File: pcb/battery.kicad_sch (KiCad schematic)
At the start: 16 parts, among them J1 Battery_JST, J2 Battery_JST, Q1 FS8205A, U1 IP2326, U2 HY2120CB, U5 TPS54308

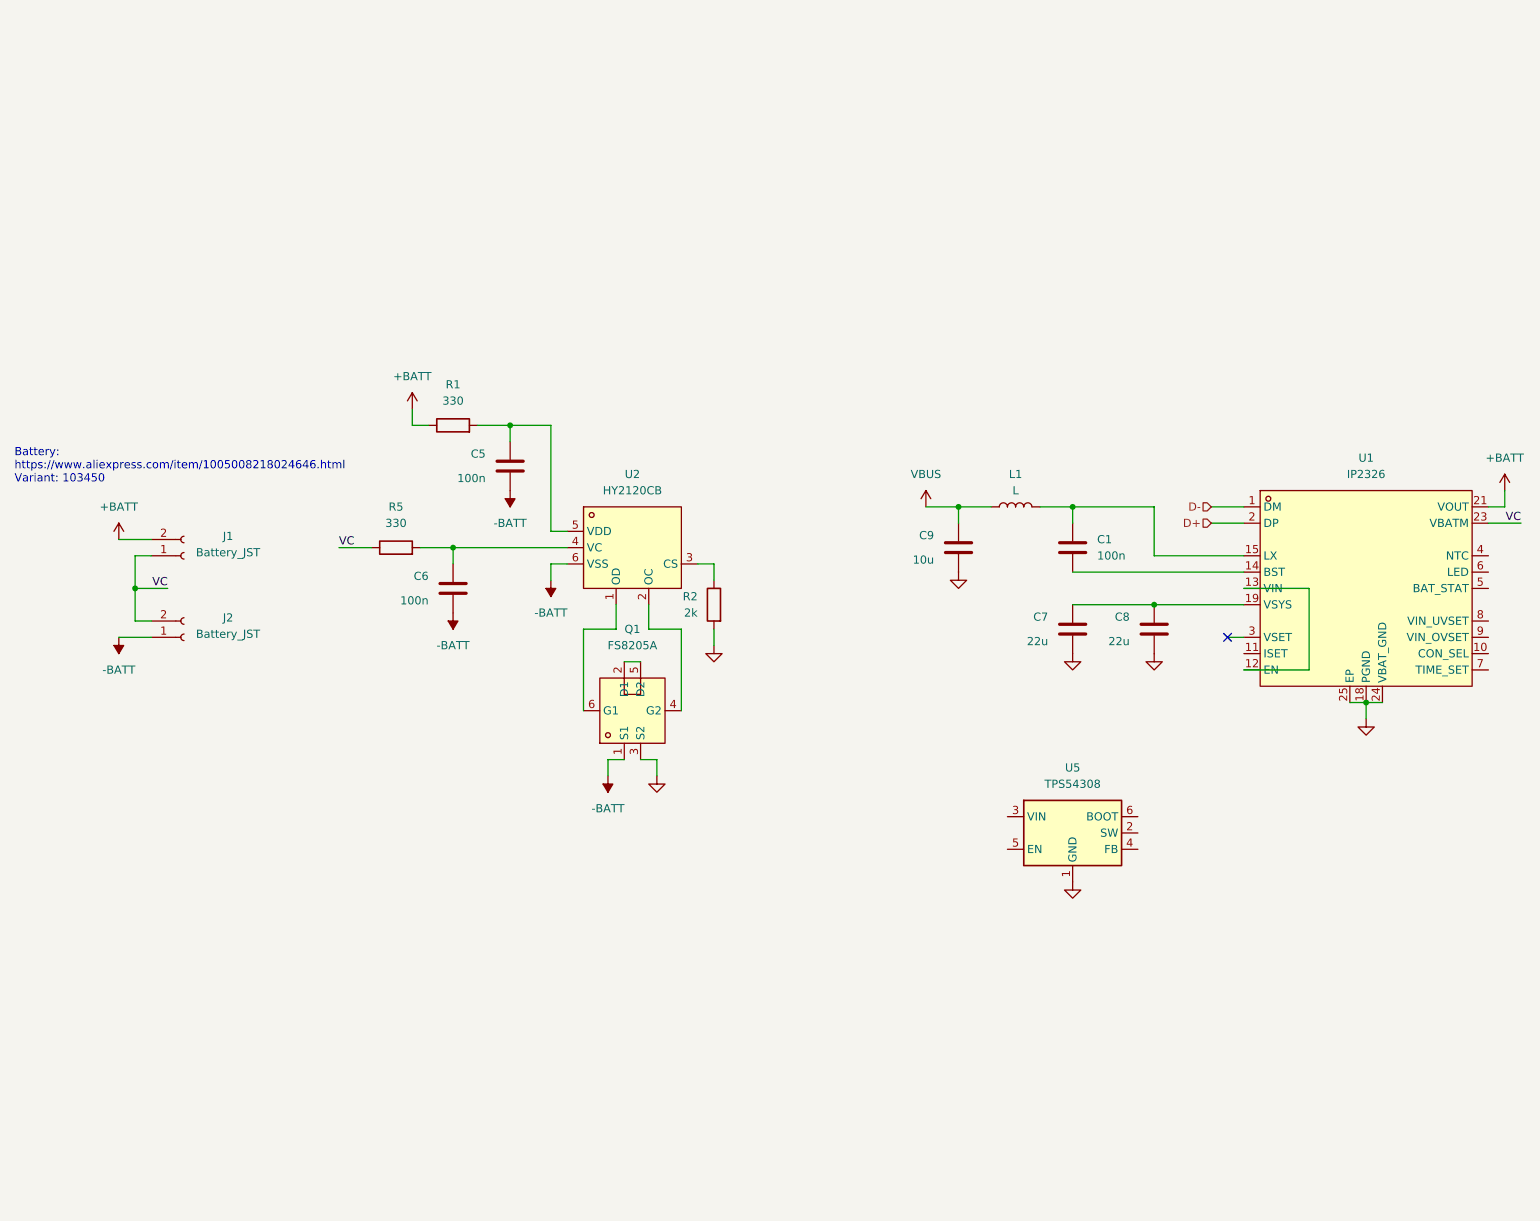
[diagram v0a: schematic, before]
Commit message: add neopixel sheet, finished battery and main circuitry
Signed-off-by: Toby Cm <toby@vsus.app>
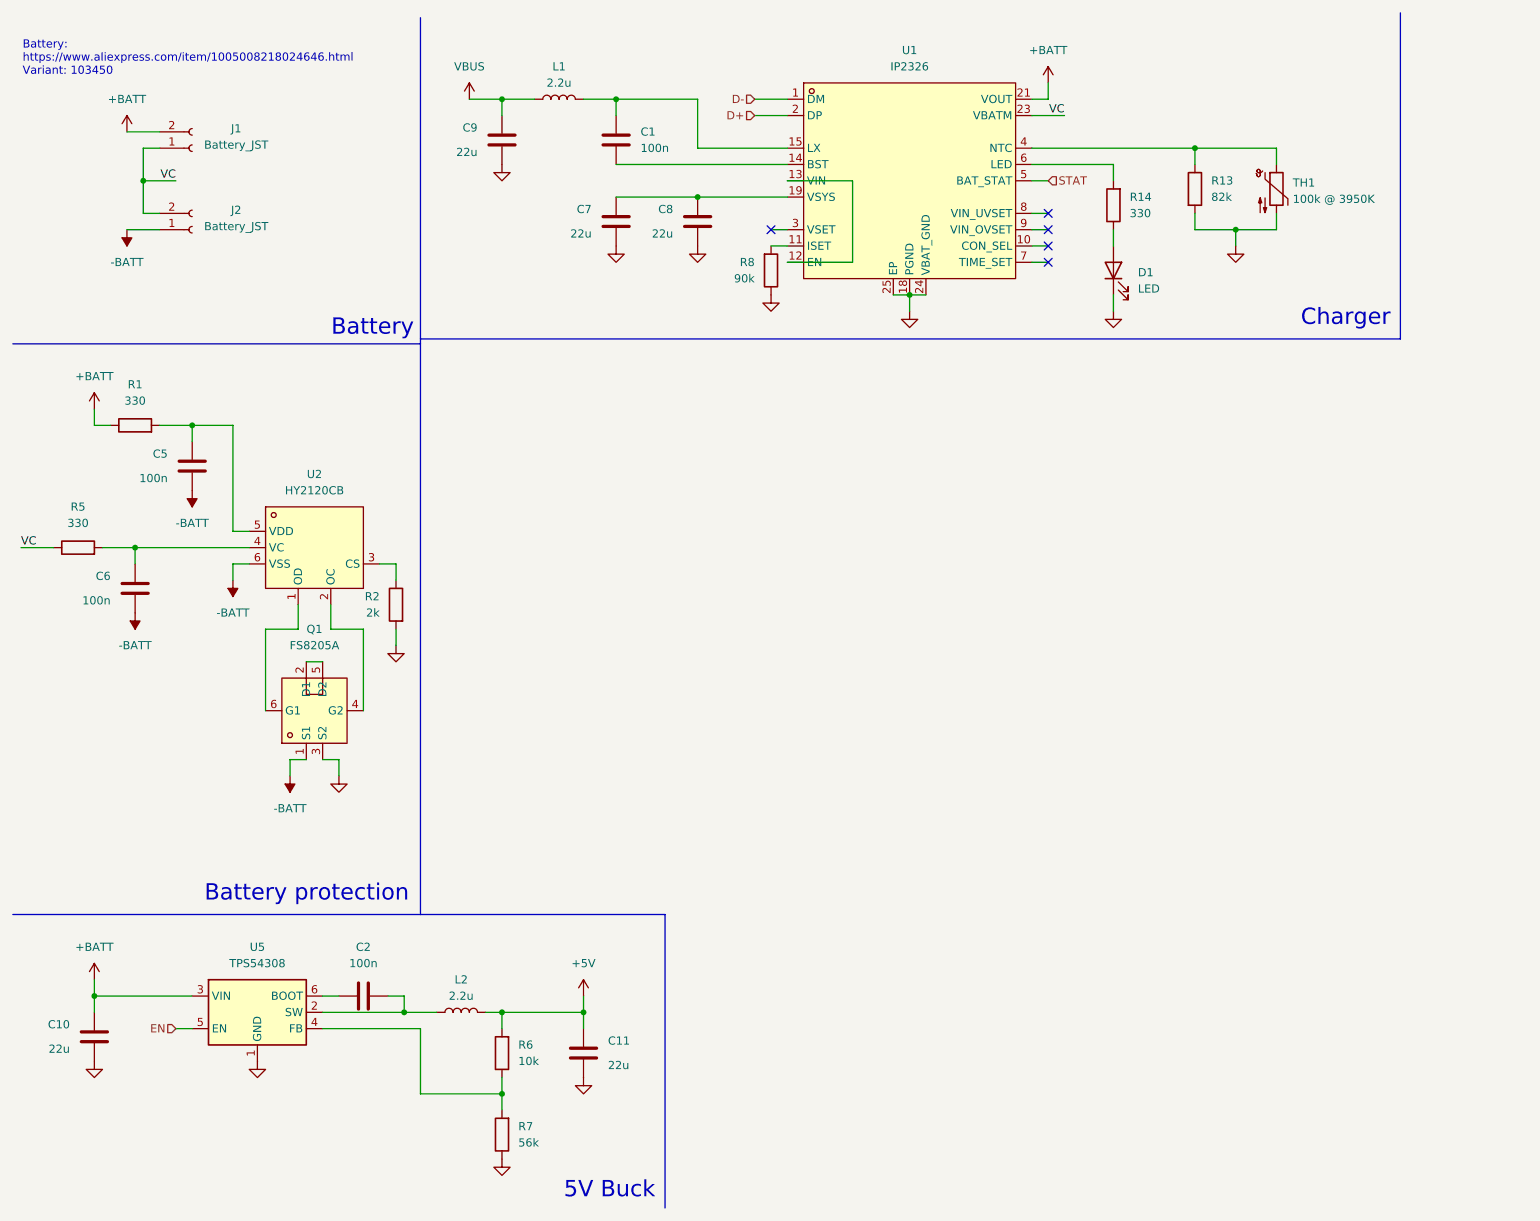
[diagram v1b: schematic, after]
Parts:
- added C10, C11: 22u, Capacitor_SMD:C_0805_2012Metric, symbol Device:C
- added C2: 100n, Capacitor_SMD:C_0603_1608Metric, symbol Device:C
- added D1: LED, LED_SMD:LED_0603_1608Metric, symbol Device:LED
- added L2: 2.2u, Inductor_SMD:L_APV_APH0630, symbol Device:L
- added R13: 82k, Resistor_SMD:R_0603_1608Metric, symbol Device:R
- added R14: 330, Resistor_SMD:R_0603_1608Metric, symbol Device:R
- added R6: 10k, Resistor_SMD:R_0603_1608Metric, symbol Device:R
- added R7: 56k, Resistor_SMD:R_0603_1608Metric, symbol Device:R
- added R8: 90k, Resistor_SMD:R_1206_3216Metric, symbol Device:R
- added TH1: 100k @ 3950K, Resistor_SMD:R_0603_1608Metric, symbol Device:Thermistor_NTC
- C5, C6: LCSC Part C1590 -> C1591
- C7, C8: LCSC Part C296720 -> C602037
- C9: value 10u -> 22u; footprint Capacitor_SMD:C_0603_1608Metric -> Capacitor_SMD:C_0805_2012Metric; LCSC Part C85713 -> C602037
- L1: value L -> 2.2u; footprint (none) -> Inductor_SMD:L_APV_APH0630; LCSC Part (none) -> C5349701
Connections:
- net +BATT: now also U5.3 (VIN), C10.1
- net GND: now also C10.2, C11.2, D1.1 (K), R13.2, R7.1, R8.1, TH1.2
- net at U5.2 (SW): now also C2.2, L2.1
- net at U5.4 (FB): now also R6.1, R7.2
- net EN: now reaches U5.5 (EN)
- net at U5.6 (BOOT): now also C2.1
- net at U1.11 (ISET): now also R8.2
- net at U1.4 (NTC): now also R13.1, TH1.1
- net STAT: now reaches U1.5 (BAT_STAT)
- net at U1.6 (LED): now also R14.2
- new net: D1.2 (A), R14.1
- new net +5V: C11.1, L2.2, R6.2
- no-connect marks 1 -> 5
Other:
- note added: "5V Buck"
- note added: "Battery"
- note added: "Battery protection"
- note added: "Charger"
- moved on the sheet: C1, C5, C6, C7, C8, J1, J2, L1, Q1, R1, R2, R5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

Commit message: initial pcb routing done
Signed-off-by: Toby Cm <toby@vsus.app>
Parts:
- added C14: 22u, Capacitor_SMD:C_0805_2012Metric, symbol Device:C
- added U6: SS12D10G6-WJ, easyeda2kicad:SW-TH_3P-P4.80_HX-SS12D10G6-WJ, symbol easyeda2kicad:SS12D10G6-WJ
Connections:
- net +BATT: now also C14.1, U6.1; no longer J1.2 (Pin_2)
- net GND: now also C14.2
- new net: J1.2 (Pin_2), U6.2, U6.3
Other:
- moved on the sheet: J1, J2
